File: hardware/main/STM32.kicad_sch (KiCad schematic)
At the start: 26 parts, among them U202 REF3430QDGKRQ1, U203 STM32L431RCTx

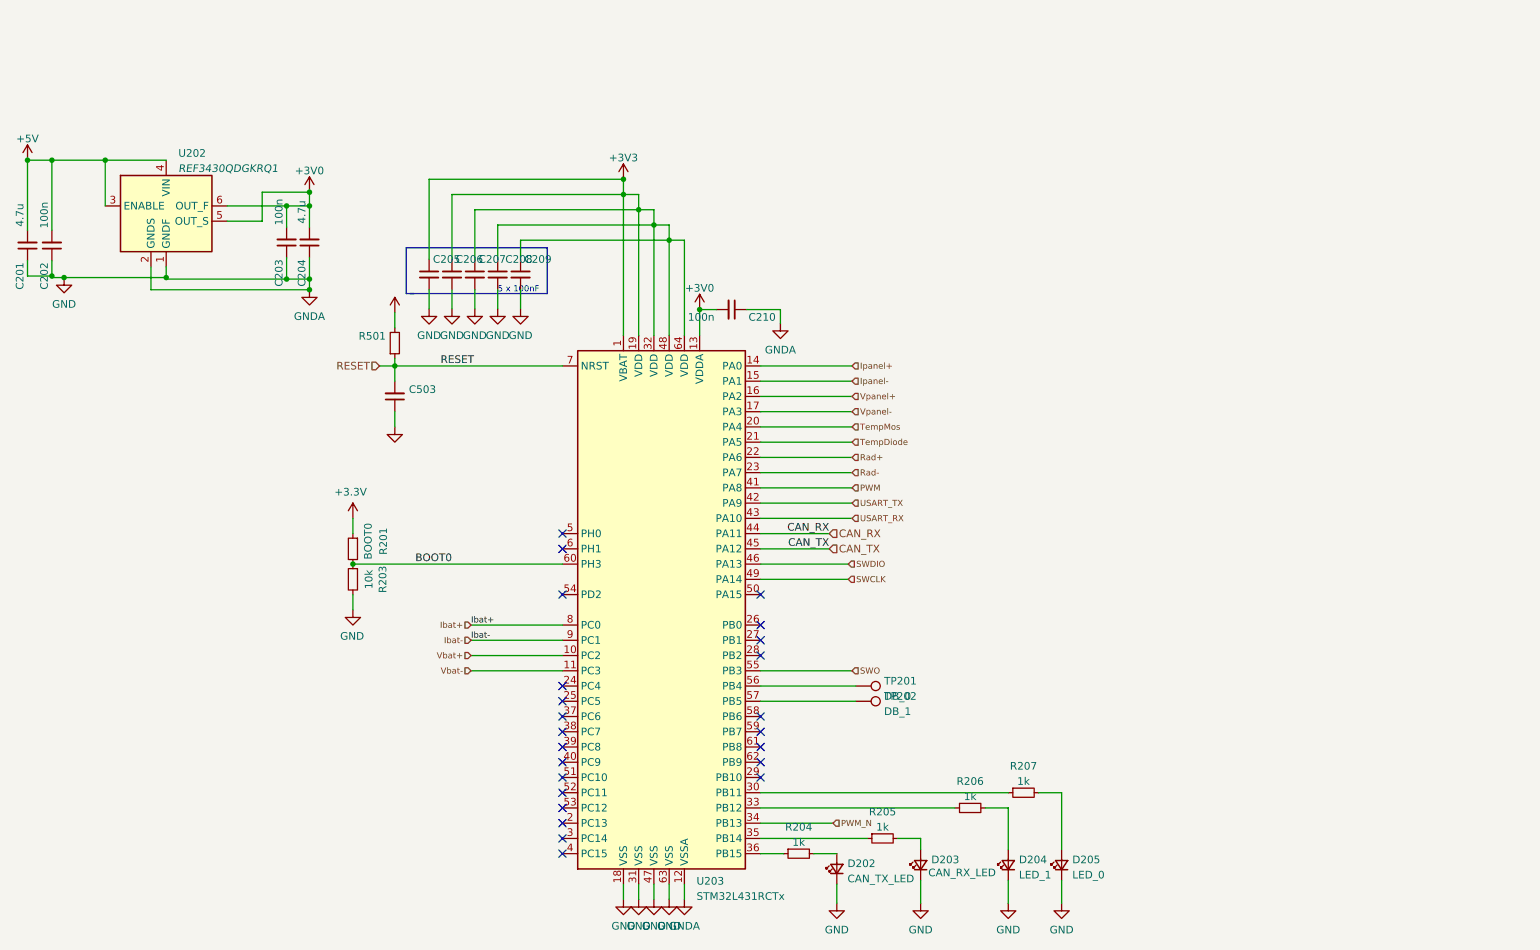
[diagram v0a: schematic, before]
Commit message: Schematics: finalize Analog Snubber and Supplies
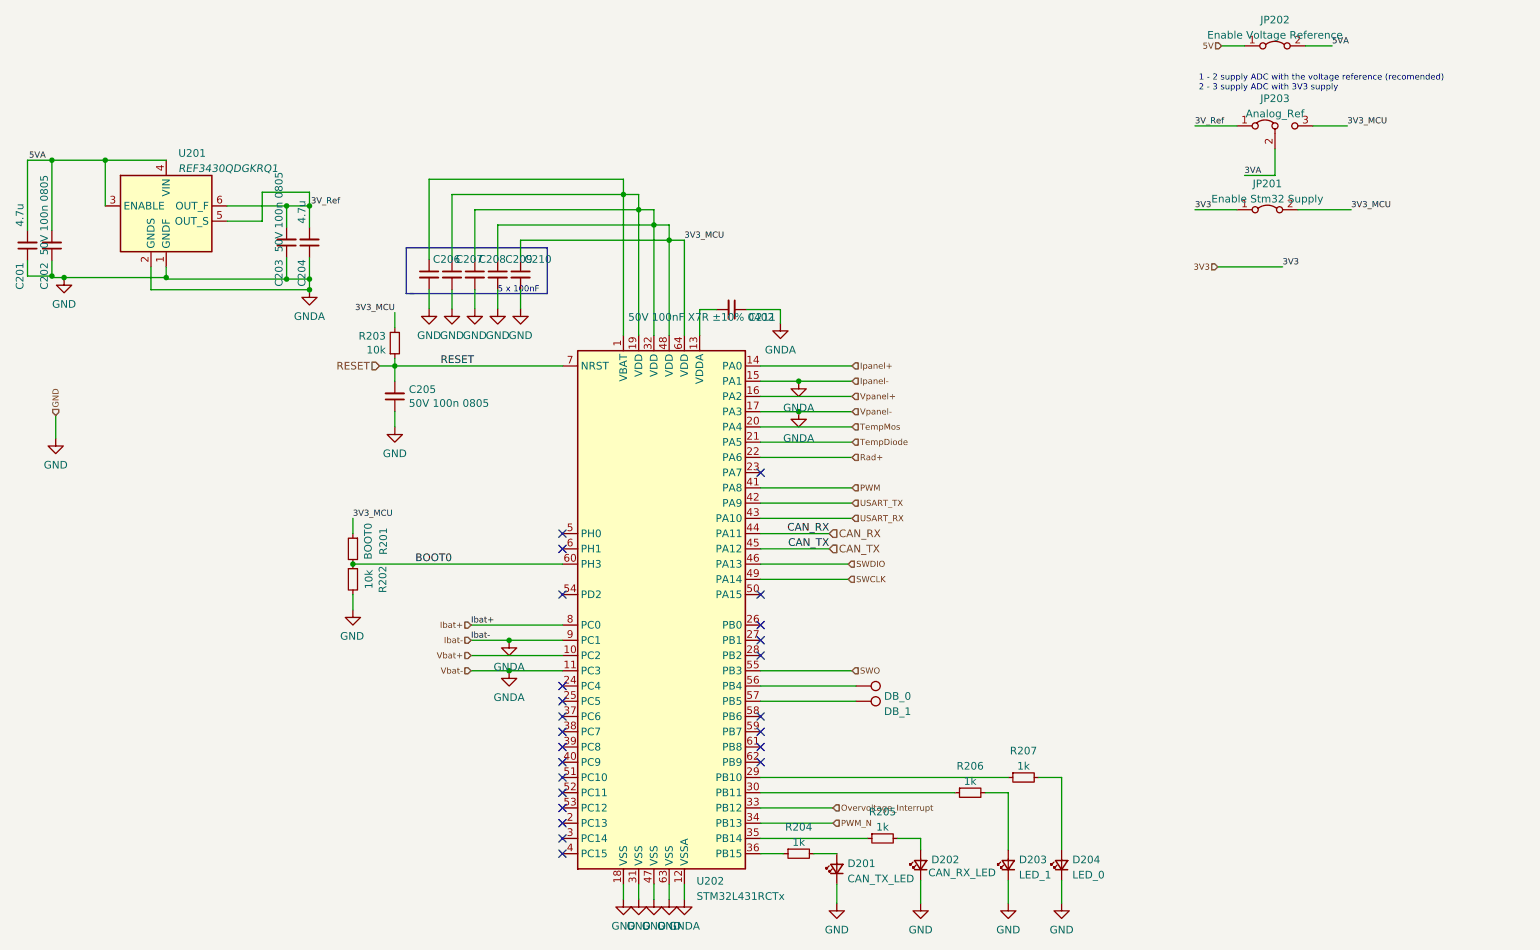
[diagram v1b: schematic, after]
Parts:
- added JP201: Enable Stm32 Supply, symbol Jumper:Jumper_2_Bridged
- added JP202: Enable Voltage Reference, symbol Jumper:Jumper_2_Bridged
- added JP203: Analog_Ref, symbol Jumper:Jumper_3_Bridged12
- C202, C203: value 100n -> 50V 100n 0805
- C205: renamed from C503; value ~ -> 50V 100n 0805
- C206: renamed from C205; value 100n -> 50V 100nF X7R ±10% 0402
- C207: renamed from C206; value C_Small -> 50V 100nF X7R ±10% 0402
- C208: renamed from C207; value C_Small -> 50V 100nF X7R ±10% 0402
- C209: renamed from C208; value C_Small -> 50V 100nF X7R ±10% 0402
- C210: renamed from C209; value C_Small -> 50V 100nF X7R ±10% 0402
- C211: renamed from C210; value 100n -> 50V 100nF X7R ±10% 0402
- R203: renamed from R501; value ~ -> 10k
- renumbered D202 to D201, D203 to D202, D204 to D203, D205 to D204, R203 to R202, U202 to U201, U203 to U202
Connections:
- net Ibat- is gone; now on net GND: U202.9 (PC1)
- net Ipanel- is gone; now on net GND: U202.15 (PA1)
- net Vbat- is gone; now on net GND: U202.11 (PC3)
- net Vpanel- is gone; now on net GND: U202.17 (PA3)
- net at R207.1: now also U202.29 (PB10); no longer U202.30 (PB11)
- net at R206.1: now also U202.30 (PB11); no longer U202.33 (PB12)
- net +3V0 renamed 3V_Ref
- net 3V_Ref: now also JP203.1 (A); no longer C211.2, U202.13 (VDDA)
- net +3V3 renamed 3V3_MCU
- net 3V3_MCU: now also JP201.2 (B), JP203.3 (B)
- net +5V renamed 5VA
- net 5VA: now also JP202.2 (B)
- net Rad-: no longer names the net of U202.23 (PA7)
- new net: C211.2, U202.13 (VDDA)
- new net 3V3: JP201.1 (A)
- new net 3VA: JP203.2 (C)
- new net 5V: JP202.1 (A)
- new net Overvoltage_Interrupt: U202.33 (PB12)
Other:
- note added: "1 - 2 supply ADC with the voltage reference (recomended) 2 - 3 supply ADC with 3V3 supply"
- moved on the sheet: R206, R207

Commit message: Schematics: Modified component values
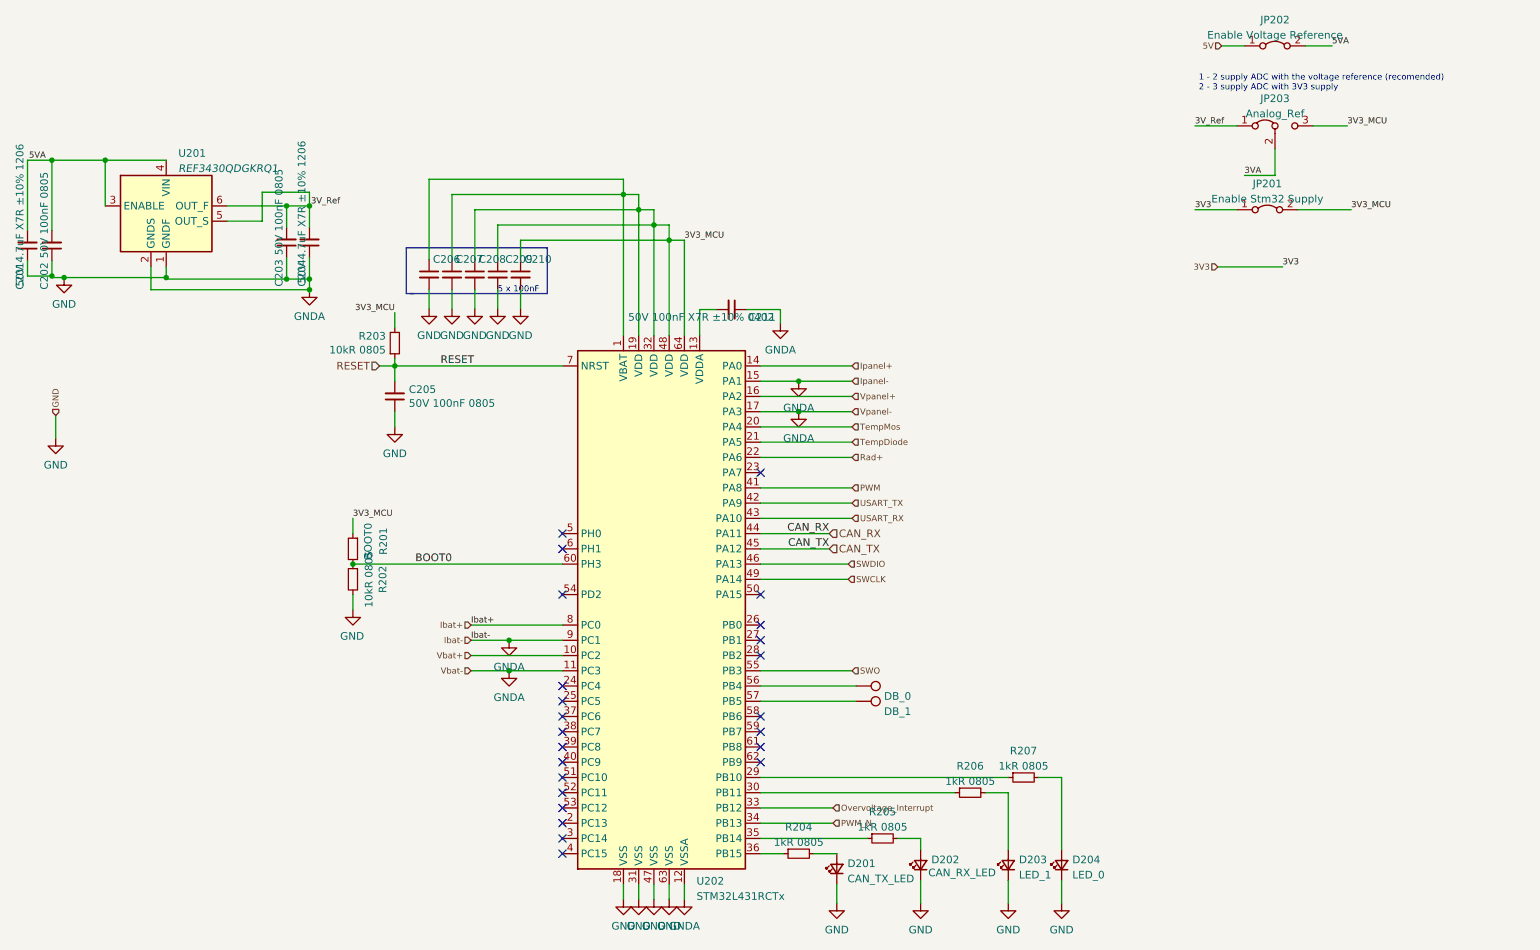
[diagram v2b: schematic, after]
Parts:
- C201, C204: value 4.7u -> 50V 4.7uF X7R ±10% 1206
- C202, C203, C205: value 50V 100n 0805 -> 50V 100nF 0805
- R202: value 10k -> 10kR 0805; footprint Resistor_SMD:R_0603_1608Metric_Pad0.98x0.95mm_HandSolder -> Resistor_SMD:R_0805_2012Metric_Pad1.20x1.40mm_HandSolder
- R203: value 10k -> 10kR 0805
- R204, R205, R206, R207: value 1k -> 1kR 0805
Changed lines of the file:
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@@
       (effects (font (size 1.27 1.27)) (justify right))
     )
-    (property "Value" "50V 100n 0805" (id 1) (at 96.9518 82.423 0)
+    (property "Value" "50V 100nF 0805" (id 1) (at 96.9518 82.423 0)
       (effects (font (size 1.27 1.27)) (justify right))
     )
@@
       (effects (font (size 1.27 1.27)) (justify right))
     )
-    (property "Value" "10k" (id 1) (at 93.1164 73.533 0)
+    (property "Value" "10kR 0805" (id 1) (at 93.1164 73.533 0)
       (effects (font (size 1.27 1.27)) (justify right))
     )
@@
     (in_bom yes) (on_board yes)
     (property "Reference" "C201" (id 0) (at 32.131 61.214 90))
-    (property "Value" "4.7u" (id 1) (at 32.131 51.054 90))
+    (property "Value" "50V 4.7uF X7R ±10% 1206" (id 1) (at 32.131 51.054 90))
     (property "Footprint" "" (id 2) (at 33.401 56.134 0)
       (effects (font (size 1.27 1.27)) hide)
@@
     (in_bom yes) (on_board yes) (fields_autoplaced)
     (property "Reference" "R205" (id 0) (at 175.895 150.5036 90))
-    (property "Value" "1k" (id 1) (at 175.895 153.0405 90))
+    (property "Value" "1kR 0805" (id 1) (at 175.895 153.0405 90))
     (property "Footprint" "" (id 2) (at 175.895 154.94 0)
       (effects (font (size 1.27 1.27)) hide)
@@
     (in_bom yes) (on_board yes)
     (property "Reference" "C203" (id 0) (at 75.311 60.706 90))
-    (property "Value" "50V 100n 0805" (id 1) (at 75.311 50.546 90))
+    (property "Value" "50V 100nF 0805" (id 1) (at 75.311 50.546 90))
     (property "Footprint" "" (id 2) (at 76.581 55.626 0)
       (effects (font (size 1.27 1.27)) hide)
@@
     (in_bom yes) (on_board yes) (fields_autoplaced)
     (property "Reference" "R207" (id 0) (at 199.39 140.3436 90))
-    (property "Value" "1k" (id 1) (at 199.39 142.8805 90))
+    (property "Value" "1kR 0805" (id 1) (at 199.39 142.8805 90))
     (property "Footprint" "" (id 2) (at 199.39 144.78 0)
       (effects (font (size 1.27 1.27)) hide)
@@
     (in_bom yes) (on_board yes) (fields_autoplaced)
     (property "Reference" "R206" (id 0) (at 190.5 142.8836 90))
-    (property "Value" "1k" (id 1) (at 190.5 145.4205 90))
+    (property "Value" "1kR 0805" (id 1) (at 190.5 145.4205 90))
     (property "Footprint" "" (id 2) (at 190.5 147.32 0)
       (effects (font (size 1.27 1.27)) hide)
@@
     (in_bom yes) (on_board yes)
     (property "Reference" "R202" (id 0) (at 92.6084 111.76 90))
-    (property "Value" "10k" (id 1) (at 90.297 111.76 90))
-    (property "Footprint" "Resistor_SMD:R_0603_1608Metric_Pad0.98x0.95mm_HandSolder" (id 2) (at 87.63 111.76 0)
+    (property "Value" "10kR 0805" (id 1) (at 90.297 111.76 90))
+    (property "Footprint" "Resistor_SMD:R_0805_2012Metric_Pad1.20x1.40mm_HandSolder" (id 2) (at 87.63 111.76 0)
       (effects (font (size 1.27 1.27)) hide)
     )
@@
     (in_bom yes) (on_board yes)
     (property "Reference" "C202" (id 0) (at 36.195 61.214 90))
-    (property "Value" "50V 100n 0805" (id 1) (at 36.195 51.054 90))
+    (property "Value" "50V 100nF 0805" (id 1) (at 36.195 51.054 90))
     (property "Footprint" "" (id 2) (at 37.465 56.134 0)
       (effects (font (size 1.27 1.27)) hide)
@@
     (in_bom yes) (on_board yes) (fields_autoplaced)
     (property "Reference" "R204" (id 0) (at 161.925 153.0436 90))
-    (property "Value" "1k" (id 1) (at 161.925 155.5805 90))
+    (property "Value" "1kR 0805" (id 1) (at 161.925 155.5805 90))
     (property "Footprint" "" (id 2) (at 161.925 157.48 0)
       (effects (font (size 1.27 1.27)) hide)
@@
     (in_bom yes) (on_board yes)
     (property "Reference" "C204" (id 0) (at 79.121 60.706 90))
-    (property "Value" "4.7u" (id 1) (at 79.121 50.546 90))
+    (property "Value" "50V 4.7uF X7R ±10% 1206" (id 1) (at 79.121 50.546 90))
     (property "Footprint" "" (id 2) (at 80.391 55.626 0)
       (effects (font (size 1.27 1.27)) hide)

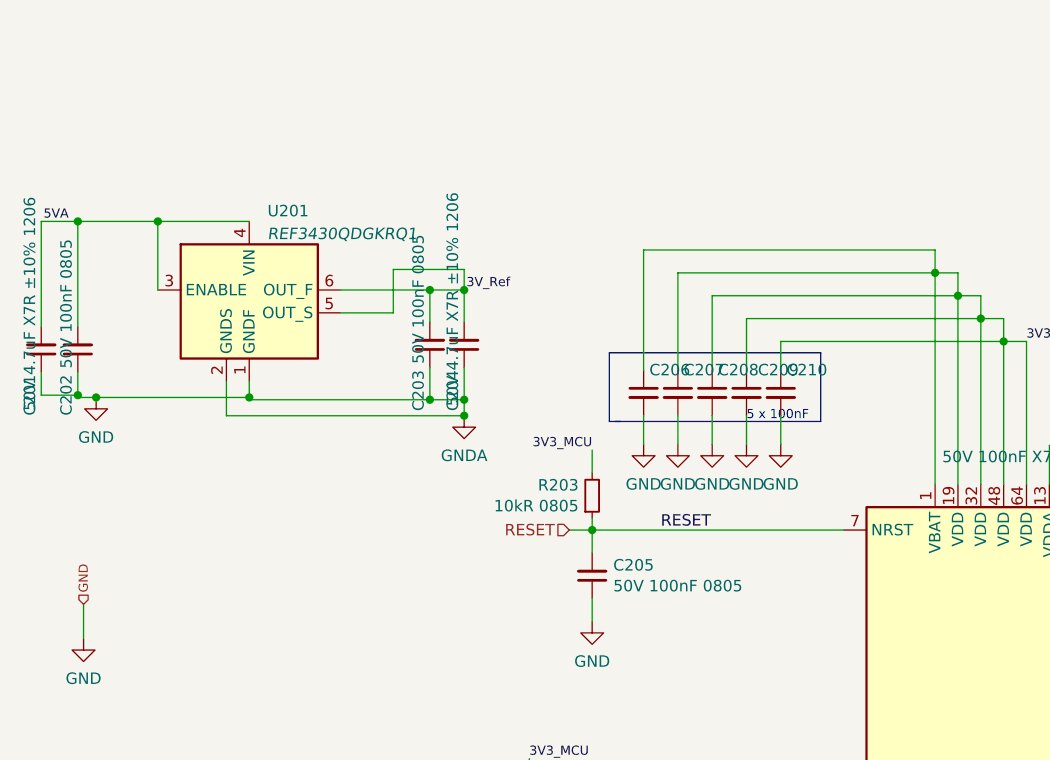
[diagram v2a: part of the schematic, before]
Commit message: Schematics: Sym table and libs updated
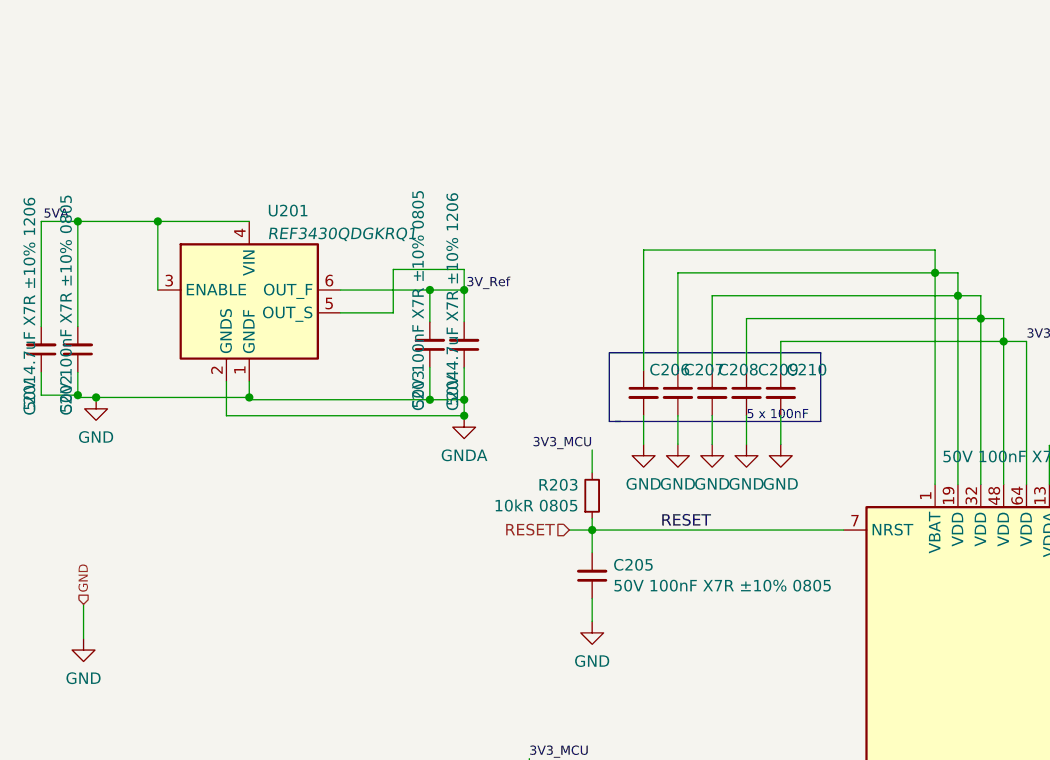
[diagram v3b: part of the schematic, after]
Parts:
- C202, C203, C205: value 50V 100nF 0805 -> 50V 100nF X7R ±10% 0805
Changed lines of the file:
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@@
       (effects (font (size 1.27 1.27)) (justify right))
     )
-    (property "Value" "50V 100nF 0805" (id 1) (at 96.9518 82.423 0)
+    (property "Value" "50V 100nF X7R ±10% 0805" (id 1) (at 96.9518 82.423 0)
       (effects (font (size 1.27 1.27)) (justify right))
     )
@@
     (in_bom yes) (on_board yes)
     (property "Reference" "C203" (id 0) (at 75.311 60.706 90))
-    (property "Value" "50V 100nF 0805" (id 1) (at 75.311 50.546 90))
+    (property "Value" "50V 100nF X7R ±10% 0805" (id 1) (at 75.311 50.546 90))
     (property "Footprint" "" (id 2) (at 76.581 55.626 0)
       (effects (font (size 1.27 1.27)) hide)
@@
     (in_bom yes) (on_board yes)
     (property "Reference" "C202" (id 0) (at 36.195 61.214 90))
-    (property "Value" "50V 100nF 0805" (id 1) (at 36.195 51.054 90))
+    (property "Value" "50V 100nF X7R ±10% 0805" (id 1) (at 36.195 51.054 90))
     (property "Footprint" "" (id 2) (at 37.465 56.134 0)
       (effects (font (size 1.27 1.27)) hide)
